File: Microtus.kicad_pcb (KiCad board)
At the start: 2 copper layers, 12 parts, among them J1 Conn_01x04, J2 AVR-ISP-6, SW1 SW_Push, SW2 SW_Push, SW3 SW_Push, U1 ATtiny85V-10SU

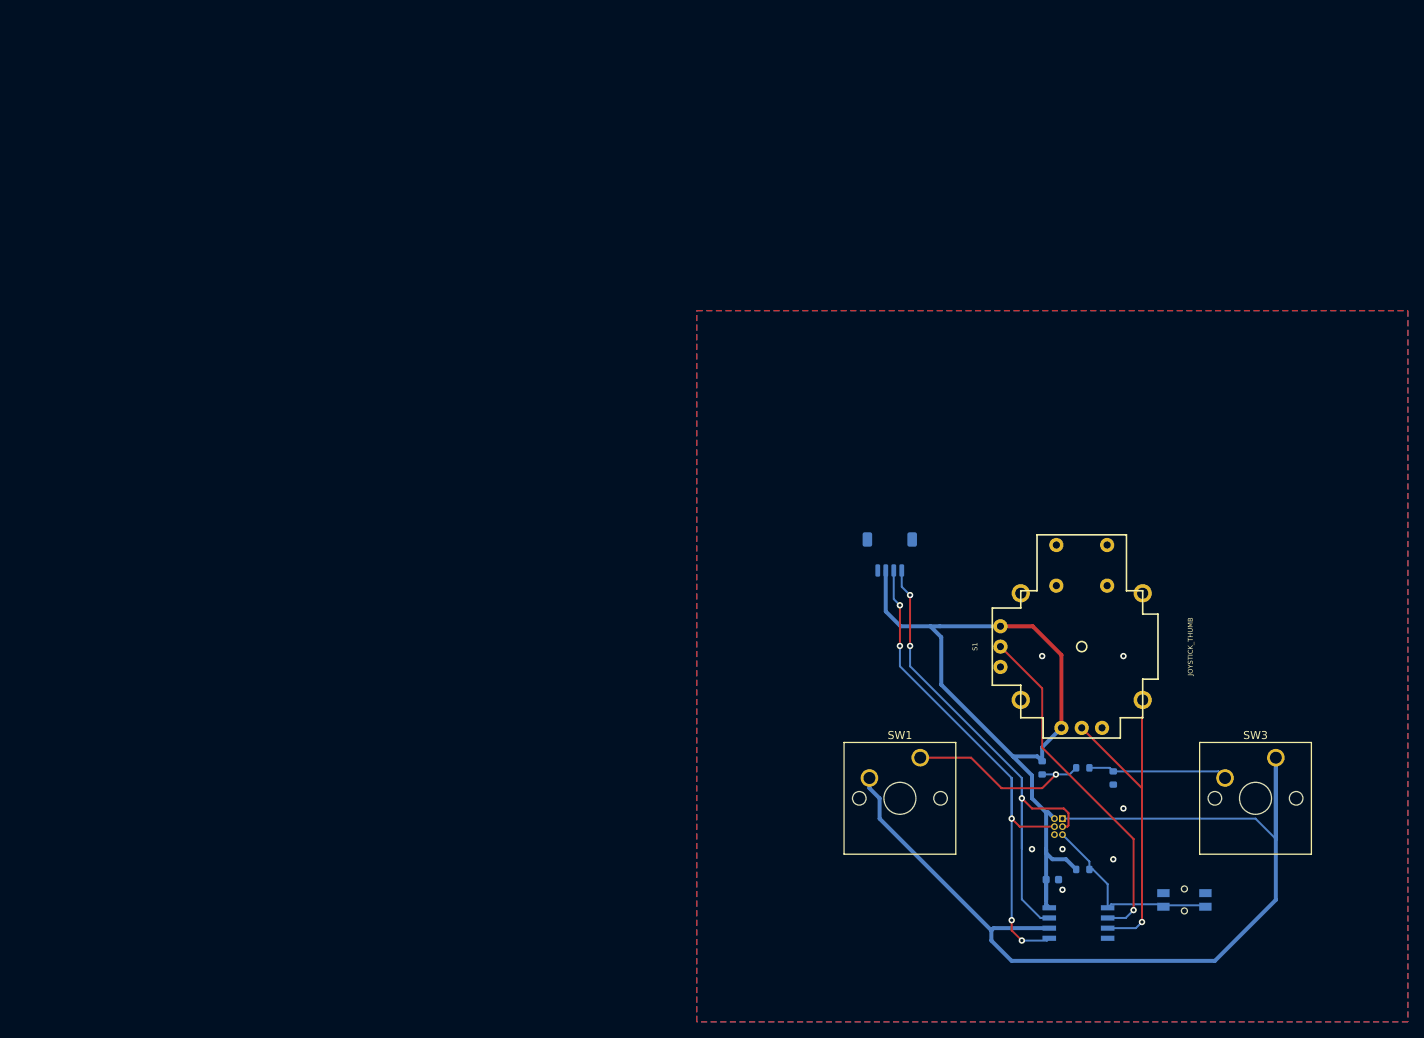
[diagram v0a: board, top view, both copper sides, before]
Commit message: go with choc switches and 0805 SMDs
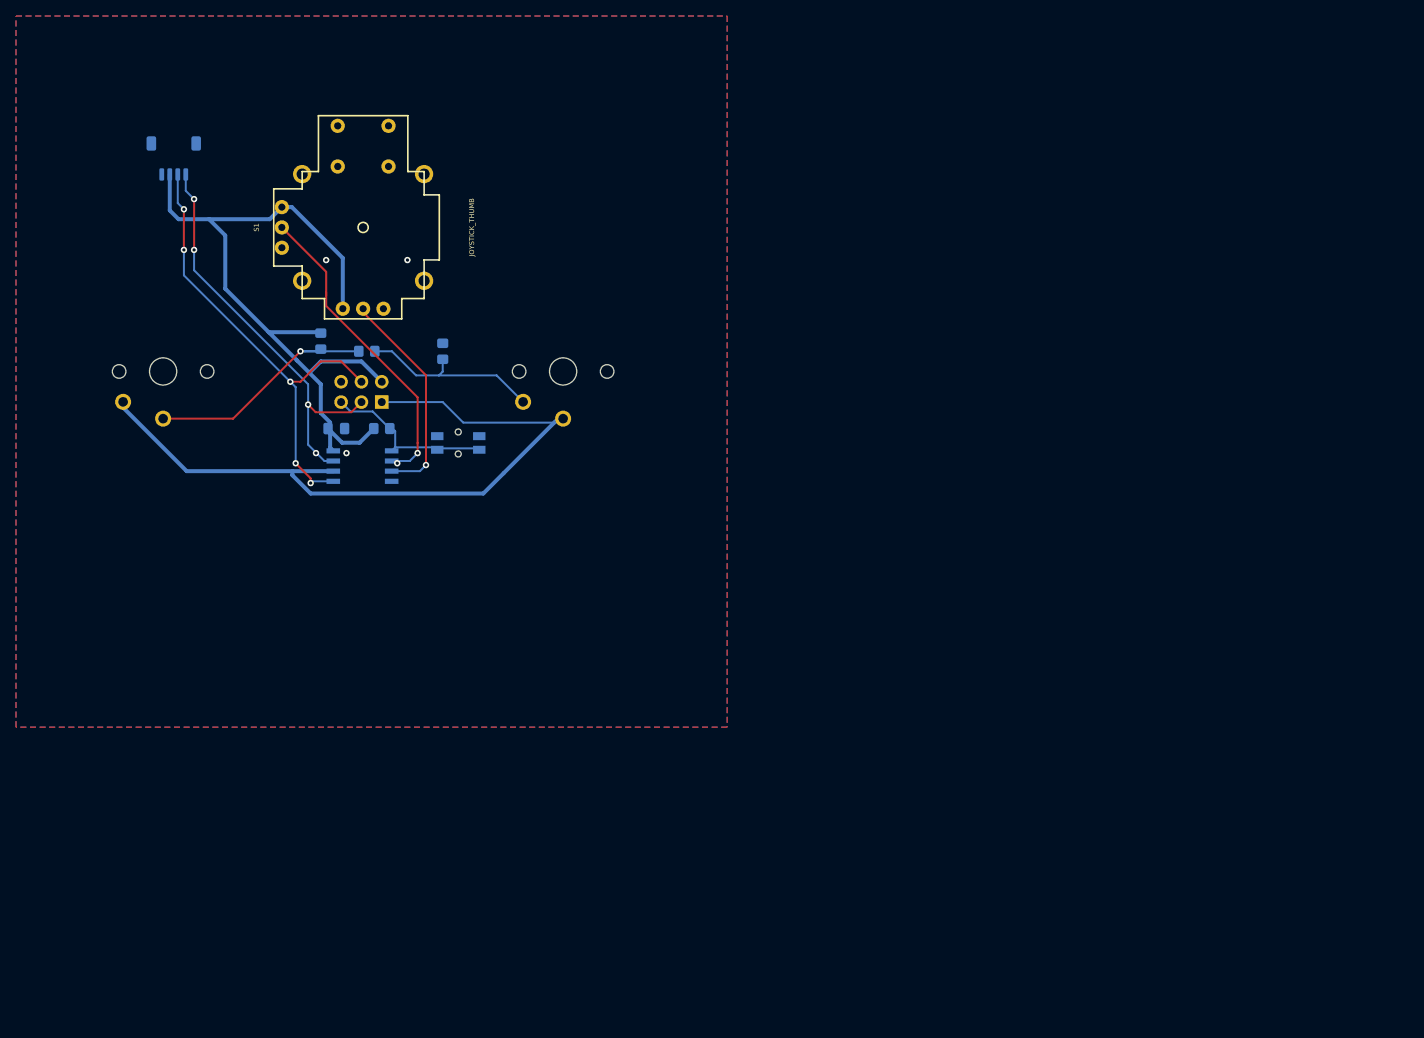
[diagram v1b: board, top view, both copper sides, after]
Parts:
- C1: footprint Capacitor_SMD:C_0603_1608Metric -> Capacitor_SMD:C_0805_2012Metric_Pad1.18x1.45mm_HandSolder
- J2: footprint Connector_PinHeader_1.00mm:PinHeader_2x03_P1.00mm_Vertical -> Connector_PinHeader_2.54mm:PinHeader_2x03_P2.54mm_Vertical
- R1, R2, R3, R4: footprint Resistor_SMD:R_0603_1608Metric -> Resistor_SMD:R_0805_2012Metric_Pad1.20x1.40mm_HandSolder
- SW1, SW3: footprint Button_Switch_Keyboard:SW_Cherry_MX_1.00u_PCB -> Keebio:Kailh-PG1350-1u-NoLED
- moved SW2 107.2 mm to (46.4, 41.9)
- moved SW1 106.2 mm to (9.50, 33.0)
- moved U1 106.2 mm to (34.4, 44.8)
- moved C1 105.8 mm to (31.1, 40.1)
- moved R2 104.8 mm to (29.2, 29.2)
- moved S1 104.0 mm to (34.5, 15.0)
- moved R3 103.5 mm to (35.0, 30.5)
- moved R1 103.5 mm to (36.8, 40.1)
- moved J1 102.3 mm to (10.8, 6.38)
- moved SW3 101.3 mm to (59.5, 33.0)
- moved J2 99.8 mm to (36.8, 36.8), turned to 90 degrees
- moved R4 99.4 mm to (44.5, 30.5), turned to 270 degrees
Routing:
- net BUTTONS: track 128.2 -> 92.7 mm
- net I2C_SCL: track 69.6 -> 51.7 mm, vias 3 -> 4
- net X_POS: track 40.9 -> 27.4 mm
- net I2C_SDA: track 67.3 -> 59.4 mm
- net Net-(R2-Pad1): track 23.8 -> 30.8 mm
- net Net-(R3-Pad1): track 17.5 -> 23.5 mm
- net Y_POS: track 43.5 -> 39.3 mm, vias 1 -> 2
- net RESET: track 24.4 -> 21.5 mm
- net +3V3: track 97.9 -> 97.2 mm
- net GND: vias 7 -> 3

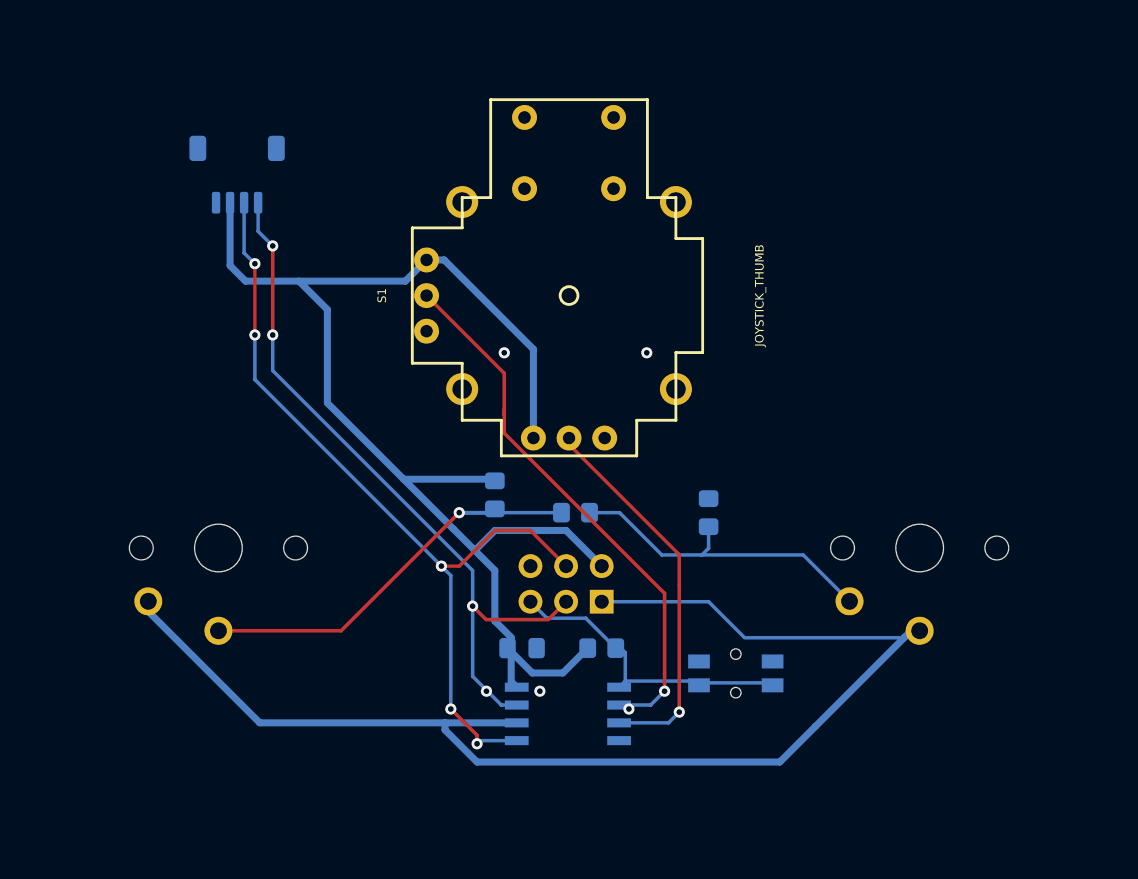
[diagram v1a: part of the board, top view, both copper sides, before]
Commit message: Shrink and switch back to 0603
also round corners with 2mm radius
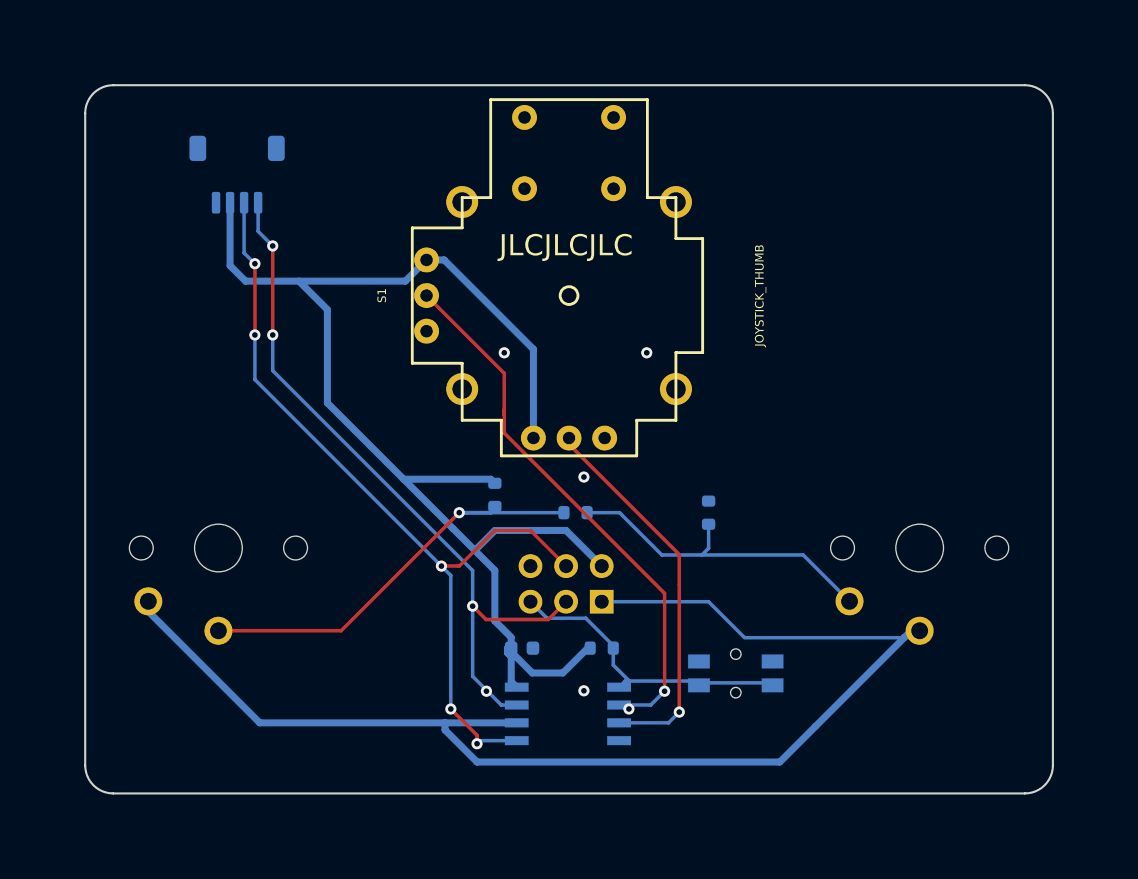
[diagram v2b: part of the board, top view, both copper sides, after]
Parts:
- C1: footprint Capacitor_SMD:C_0805_2012Metric_Pad1.18x1.45mm_HandSolder -> Capacitor_SMD:C_0603_1608Metric
- R1, R4: footprint Resistor_SMD:R_0805_2012Metric_Pad1.20x1.40mm_HandSolder -> Resistor_SMD:R_0603_1608Metric
- R2: value 2.5k -> 2.49k; footprint Resistor_SMD:R_0805_2012Metric_Pad1.20x1.40mm_HandSolder -> Resistor_SMD:R_0603_1608Metric
- R3: value 5k -> 4.99k; footprint Resistor_SMD:R_0805_2012Metric_Pad1.20x1.40mm_HandSolder -> Resistor_SMD:R_0603_1608Metric
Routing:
- net GND: vias 3 -> 4
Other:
- board outline added: 69 x 50.5 mm
- board text added: "JLCJLCJLC"

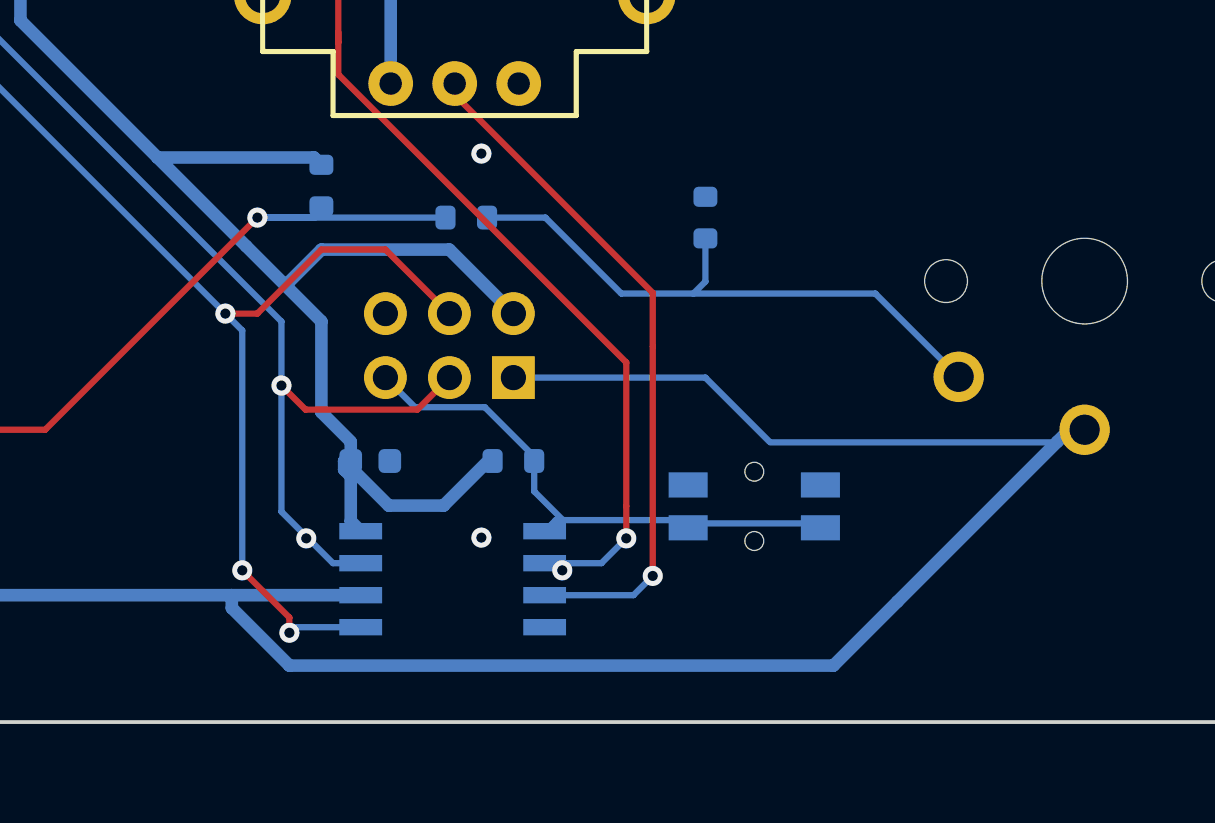
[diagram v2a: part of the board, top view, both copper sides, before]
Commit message: Add STEP files for better rendering
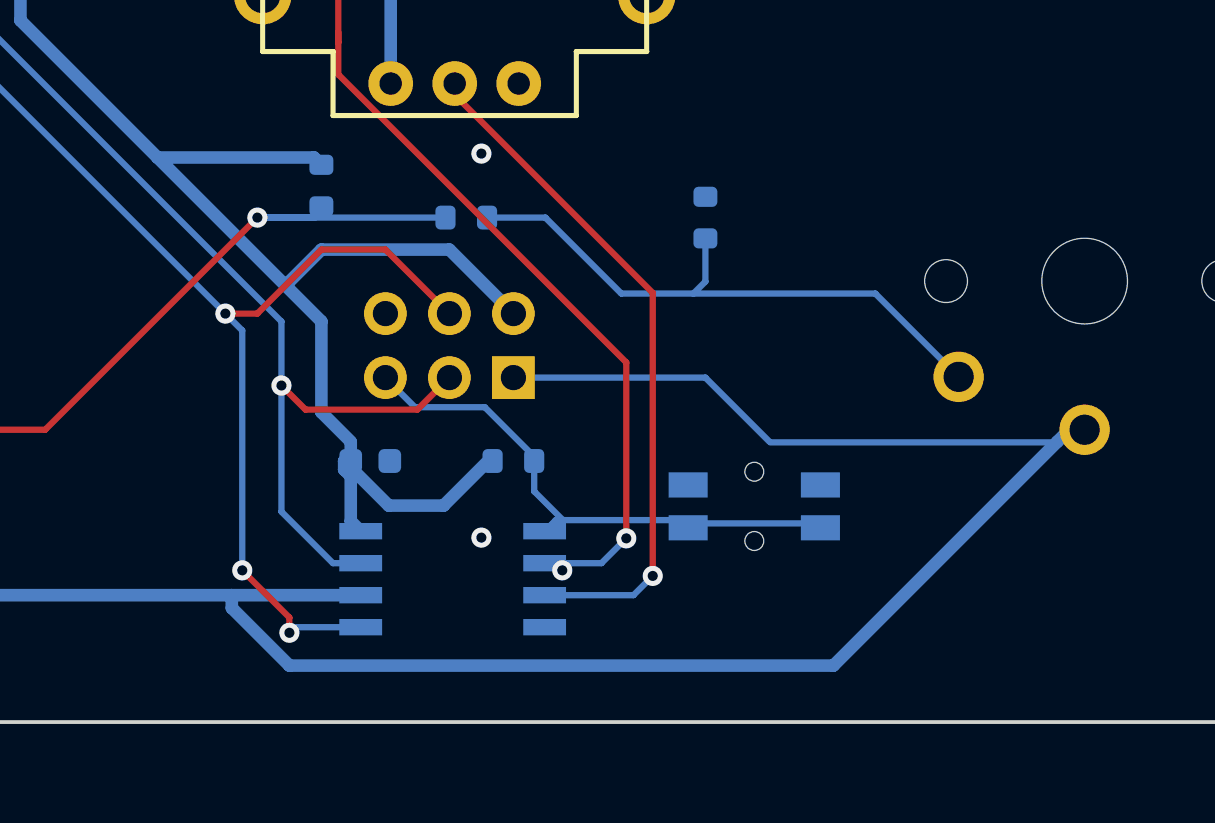
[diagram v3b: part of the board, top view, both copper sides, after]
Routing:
- net I2C_SCL: vias 4 -> 3
